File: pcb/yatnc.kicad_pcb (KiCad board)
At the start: 2 copper layers, 45 x 85 mm, 24 parts, among them J1 Conn_01x10_Socket, J3 Conn_01x02_Socket, J4 Conn_01x03_Pin, J5 Conn_02x02_Top_Bottom, J6 Conn_01x13_Socket, J7 Conn_01x13_Socket, Q1 BC547, SW1 SW_Push, U1 MAX3232

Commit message: Fix DRC errors
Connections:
- R1 pad 1: GND -> VCC
- R2 pad 2: VCC -> GND
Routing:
- net Net-(J1-Pin_8): track 45.2 -> 47.0 mm
- net VCC: track 79.3 -> 78.8 mm, vias 1 -> 0
- net GND: track 0.00 -> 0.26 mm, vias 2 -> 3

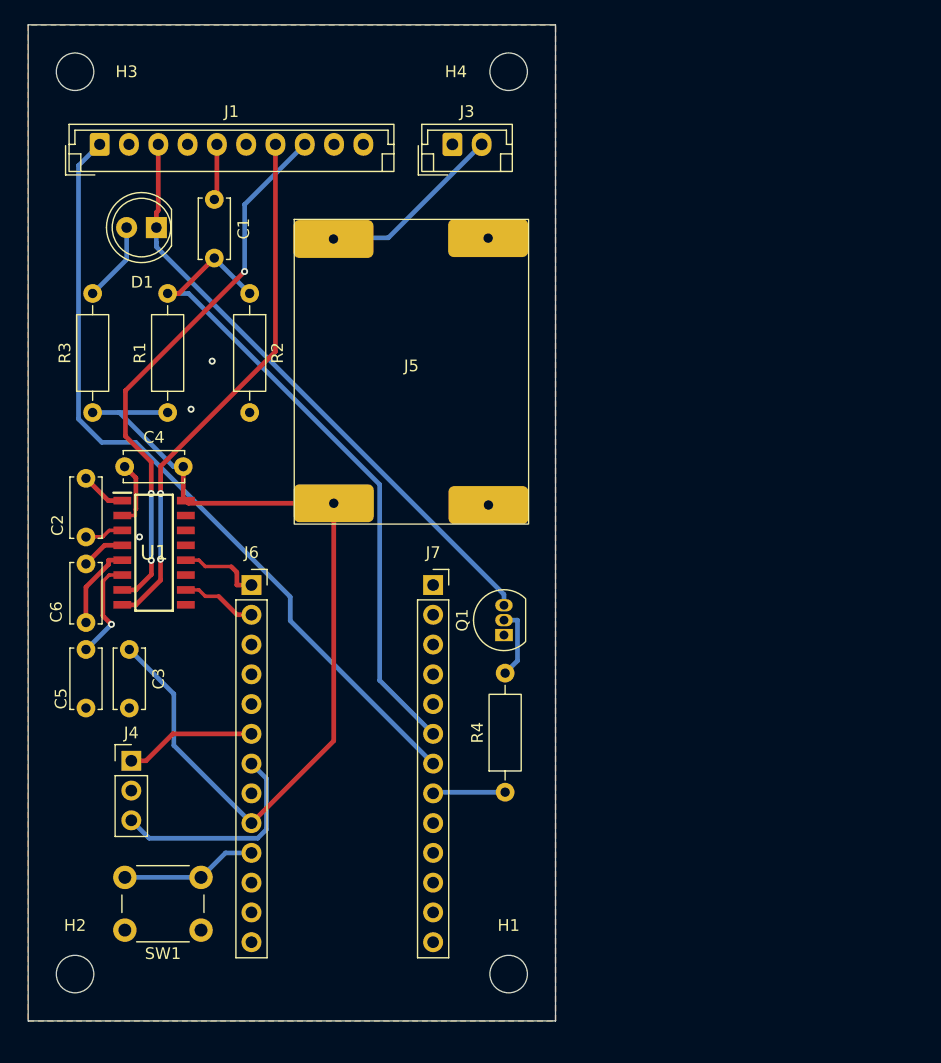
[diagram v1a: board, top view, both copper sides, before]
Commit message: add into schema 2 stage RC filter
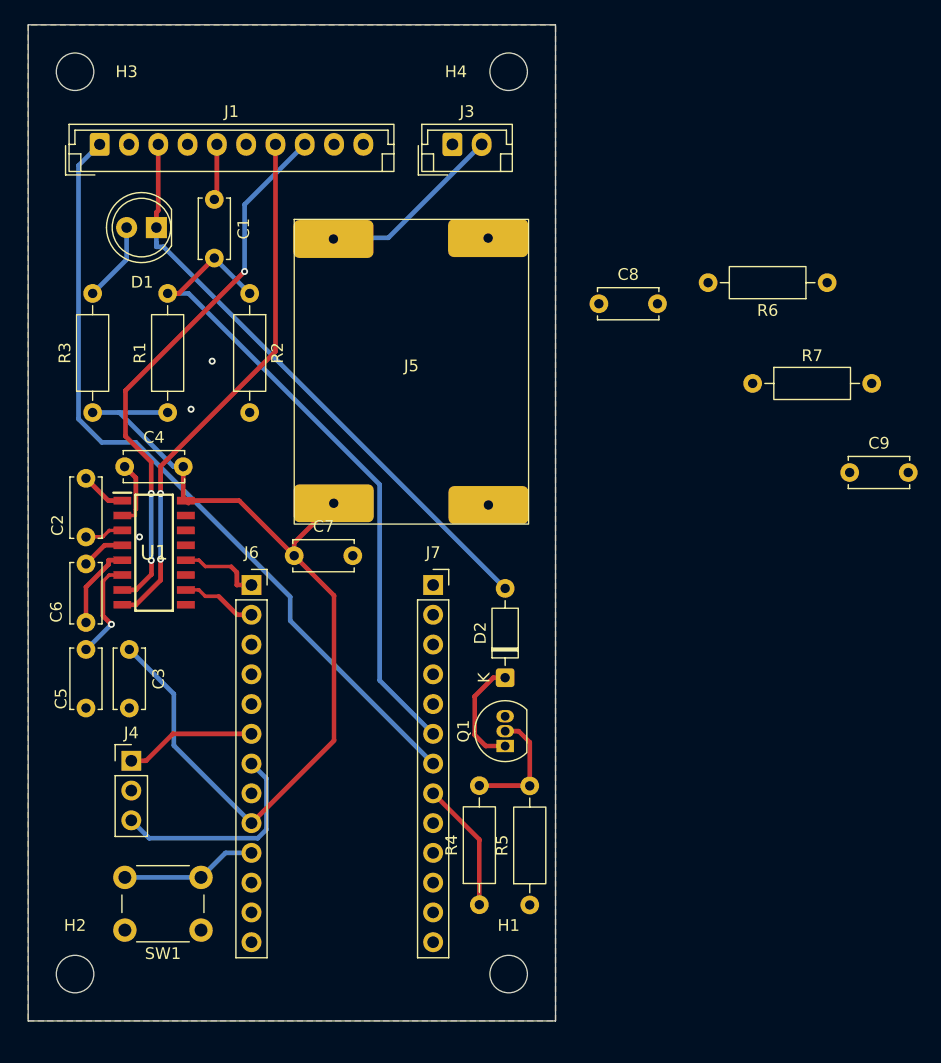
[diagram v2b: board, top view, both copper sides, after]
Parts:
- added C7: C, Capacitor_THT:C_Disc_D5.0mm_W2.5mm_P5.00mm, F.Cu at (193.2, 91.8)
- added C8: C, Capacitor_THT:C_Disc_D5.0mm_W2.5mm_P5.00mm, F.Cu at (219.2, 70.3)
- added C9: C, Capacitor_THT:C_Disc_D5.0mm_W2.5mm_P5.00mm, F.Cu at (240.6, 84.7)
- added D2: 1N4148, Diode_THT:D_DO-35_SOD27_P7.62mm_Horizontal, F.Cu at (211.2, 102.2)
- added R5: R, Resistor_THT:R_Axial_DIN0207_L6.3mm_D2.5mm_P10.16mm_Horizontal, F.Cu at (213.3, 121.6)
- added R6: R, Resistor_THT:R_Axial_DIN0207_L6.3mm_D2.5mm_P10.16mm_Horizontal, F.Cu at (238.7, 68.5)
- added R7: R, Resistor_THT:R_Axial_DIN0207_L6.3mm_D2.5mm_P10.16mm_Horizontal, F.Cu at (232.3, 77.1)
- moved R4 9.85 mm to (209.0, 121.6)
- moved Q1 9.47 mm to (211.2, 108.0)
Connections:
- J7 pad 7: Net-(J1-Pin_1) -> Net-(J7-Pin_7)
- Q1 pad 1: GND -> Net-(D2-K)
- Q1 pad 3: Net-(D1-K) -> GND
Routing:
- net Net-(D2-K): track 0.00 -> 9.55 mm
- net Net-(J7-Pin_8): track 6.19 -> 11.3 mm
- net Net-(Q1-B): track 6.11 -> 10.5 mm
- net VCC: track 78.8 -> 80.4 mm
- net Net-(D1-K): track 51.7 -> 50.6 mm

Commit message: added afsk filter and vin protection
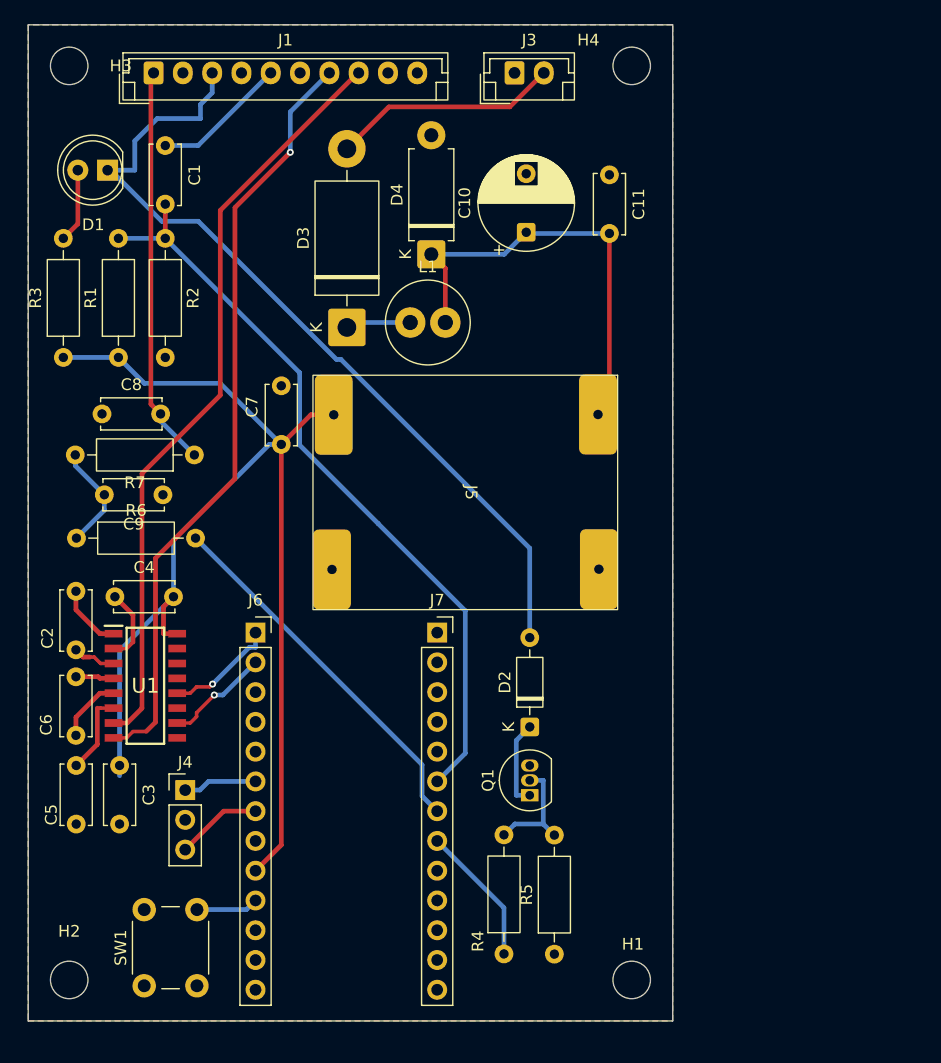
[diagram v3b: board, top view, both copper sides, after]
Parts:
- added C10: C_Polarized, Capacitor_THT:CP_Radial_D8.0mm_P5.00mm, F.Cu at (213.0, 64.2)
- added C11: C, Capacitor_THT:C_Disc_D5.0mm_W2.5mm_P5.00mm, F.Cu at (220.1, 59.3)
- added D3: 1N5822, Diode_THT:D_DO-201AD_P15.24mm_Horizontal, F.Cu at (197.7, 72.3)
- added D4: PTVS18VZ1USK, Diode_THT:D_DO-15_P10.16mm_Horizontal, F.Cu at (204.9, 66.1)
- added L1: L, Inductor_THT:L_Radial_D7.0mm_P3.00mm, F.Cu at (203.1, 71.9)
- moved R6 67.7 mm to (174.6, 90.3), turned to 0 degrees
- moved C9 58.6 mm to (182.0, 86.6), turned to 180 degrees
- moved R7 48.0 mm to (184.7, 83.2), turned to 180 degrees
- moved C8 43.4 mm to (176.8, 79.7)
- moved U1 11.4 mm to (180.5, 102.9)
- moved J5 11.3 mm to (207.8, 86.4), turned to -90 degrees
- moved C4 11.1 mm to (177.9, 95.3)
- moved H1 10.5 mm to (222.0, 128.0)
- moved H4 10.5 mm to (222.0, 50.0)
- moved C3 9.93 mm to (178.3, 109.7)
- moved C5 9.93 mm to (174.6, 109.7)
- moved C2 9.67 mm to (174.6, 94.8)
- moved C6 9.67 mm to (174.6, 102.1)
- moved C7 9.56 mm to (192.1, 82.3), turned to 90 degrees
- moved R2 8.60 mm to (182.2, 64.7)
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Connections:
- net +12V renamed Net-(D4-K)
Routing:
- net VCC: track 80.4 -> 123.2 mm
- net Net-(J1-Pin_1): track 67.8 -> 34.2 mm
- net Net-(J7-Pin_7): track 0.00 -> 31.8 mm
- net Net-(D4-K): track 15.9 -> 38.2 mm
- net Net-(D1-K): track 50.6 -> 72.1 mm
- net Net-(J1-Pin_7): track 45.4 -> 65.7 mm, vias 2 -> 1
- net Net-(J1-Pin_8): track 47.0 -> 64.9 mm, vias 3 -> 0
- net Net-(J4-Pin_3): track 18.6 -> 7.36 mm
- net Net-(C9-Pad2): track 0.00 -> 9.11 mm
- net Net-(J7-Pin_6): track 57.5 -> 64.9 mm
- net Net-(J1-Pin_5): track 4.79 -> 11.6 mm
- net Net-(J6-Pin_10): track 11.7 -> 5.32 mm
- net Net-(D3-K): track 0.00 -> 5.57 mm
- net Net-(J4-Pin_1): track 11.2 -> 6.31 mm
- net Net-(J6-Pin_2): track 6.48 -> 9.03 mm, vias 0 -> 1
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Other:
- board size 45 x 85 mm -> 55 x 85 mm

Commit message: resolve ERC/DRC. add cleaning silkscreen, add component values
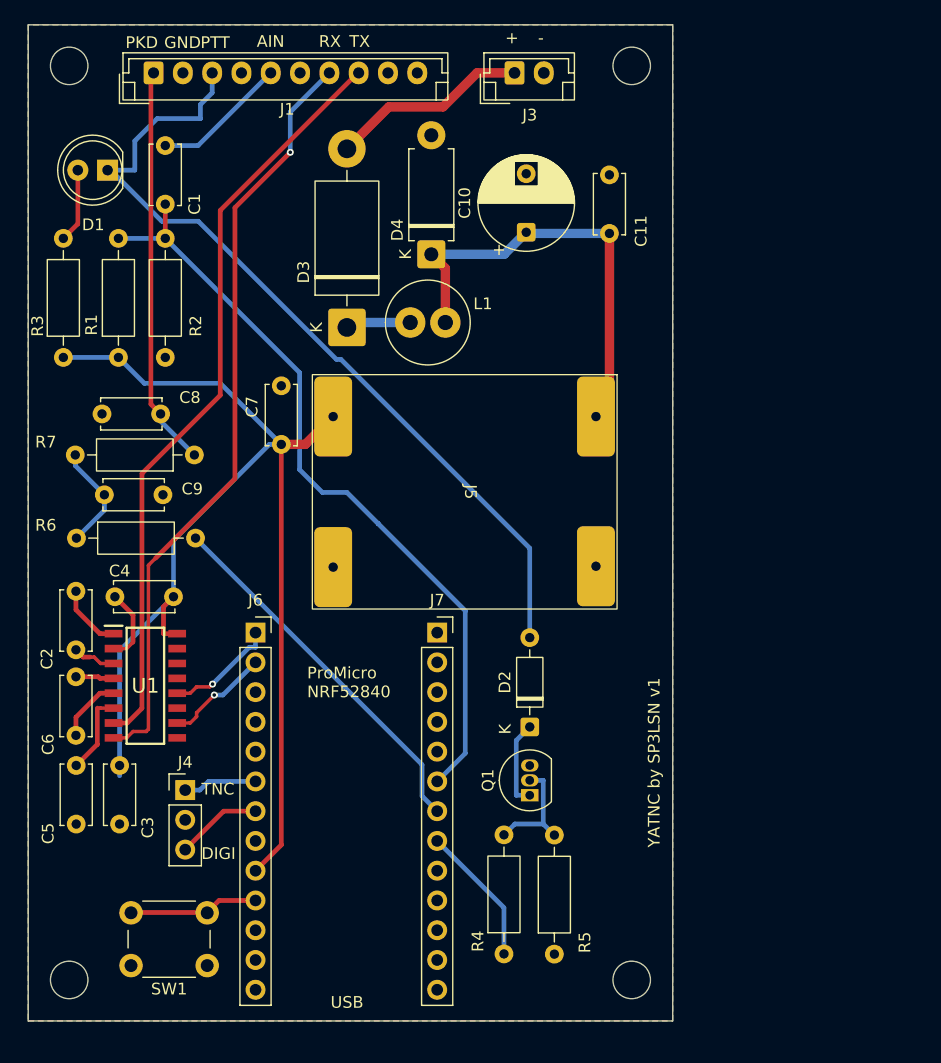
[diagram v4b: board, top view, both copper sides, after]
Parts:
- C1, C11, C2, C3, C4, C5, C6, C7: value C -> 100nF
- C10: value C_Polarized -> 470µF
- C8, C9: value C -> 4.7 nF
- D4: value PTVS18VZ1USK -> BZW04
- J5: value Conn_02x02_Top_Bottom -> DFR0570
- L1: value L -> 47µH
- R1, R2, R3, R5: value R -> 10k
- R4, R6, R7: value R -> 1k
- moved SW1 5.65 mm to (185.8, 126.8), turned to 180 degrees
- moved J5 0.07 mm to (207.8, 86.3)
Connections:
- D3 pad 2: VCC -> Net-(D3-A)
- J3 pad 1: GND -> Net-(D3-A)
- J3 pad 2: Net-(D4-K) -> GND
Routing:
- net VCC: track 123.2 -> 103.6 mm
- net Net-(D3-A): track 0.00 -> 17.0 mm
- net Net-(J6-Pin_10): track 5.32 -> 11.1 mm
- net Net-(D4-K): track 38.2 -> 36.8 mm
- net Net-(J7-Pin_6): track 64.9 -> 66.1 mm
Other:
- board text added: "+"
- board text added: "-"
- board text added: "AIN"
- board text added: "DIGI"
- board text added: "GND"
- board text added: "PKD"
- board text added: "PTT"
- board text added: "ProMicro NRF52840"
- board text added: "RX"
- board text added: "TNC"
- board text added: "TX"
- board text added: "USB"
- board text added: "YATNC by SP3LSN v1"

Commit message: first part of changes after review
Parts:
- removed L1: 47µH, Inductor_THT:L_Radial_D7.0mm_P3.00mm
- added R8: 1ohm, Resistor_THT:R_Axial_DIN0207_L6.3mm_D2.5mm_P10.16mm_Horizontal, F.Cu at (202.8, 74.2)
- D4: value BZW04 -> BZW04 18V
- J1: value Conn_01x10_Socket -> JST
- RST: renamed from SW1; value SW_Push -> RST
- moved C11 9.43 mm to (220.9, 68.7)
- moved D3 6.68 mm to (204.1, 70.4)
- moved D4 5.30 mm to (209.4, 68.9)
- moved C10 3.70 mm to (216.5, 63.0), turned to 0 degrees
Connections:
- net Net-(D1-K) renamed PTT
- net Net-(J1-Pin_1) renamed PKD
- net Net-(J1-Pin_5) renamed AUDIO IN
- net Net-(J4-Pin_1) renamed TNC
- net Net-(J4-Pin_3) renamed DIGI
- net Net-(J7-Pin_7) renamed AUDIO OUT
- net VCC renamed 3.3V
- J1 pad 7: Net-(J1-Pin_7) -> RX
- J1 pad 8: Net-(J1-Pin_8) -> TX
- U1 pad 11: unconnected-(U1-T1IN-Pad11) -> Net-(J6-Pin_2)
- U1 pad 13: unconnected-(U1-R1IN-Pad13) -> RX
- U1 pad 14: unconnected-(U1-T1OUT-Pad14) -> TX
- U1 pad 7: Net-(J1-Pin_8) -> TX
- U1 pad 8: Net-(J1-Pin_7) -> GND
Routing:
- net TX: track 0.00 -> 70.2 mm
- net Net-(J1-Pin_7): track 65.7 -> 0.00 mm, vias 1 -> 0
- net Net-(J1-Pin_8): track 64.9 -> 0.00 mm
- net RX: track 0.00 -> 64.1 mm
- net Net-(D3-A): track 17.0 -> 9.80 mm
- net Net-(D3-K): track 5.57 -> 4.31 mm
- net Net-(D4-K): track 36.8 -> 35.9 mm
- net Net-(J6-Pin_1): track 9.56 -> 8.83 mm, vias 1 -> 0
- net Net-(J6-Pin_2): track 9.03 -> 9.58 mm, vias 1 -> 0
- net GND: vias 0 -> 103

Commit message: second part of changes after review
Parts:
- removed the C7 at (192.1, 82.3)
- added C4: 100nF, Capacitor_THT:C_Disc_D5.0mm_W2.5mm_P5.00mm, F.Cu at (198.7, 124.0)
- added C6: 470µF, Capacitor_THT:CP_Radial_D8.0mm_P5.00mm, F.Cu at (199.6, 93.6)
- added POWER LED: LED, LED_THT:LED_D5.0mm, F.Cu at (177.2, 58.9)
- added R1: 10k, Resistor_THT:R_Axial_DIN0207_L6.3mm_D2.5mm_P10.16mm_Horizontal, F.Cu at (173.5, 74.8)
- BC547: renamed from Q1; footprint Package_TO_SOT_THT:TO-92_Inline -> Package_TO_SOT_THT:TO-92_Inline_Wide
- PTT LED: renamed from D1
- TO TRANSCEIVER: renamed from J1
- moved R6 27.0 mm to (219.8, 99.1), turned to -90 degrees
- moved D2 23.6 mm to (223.1, 56.4), turned to 180 degrees
- moved R2 20.5 mm to (221.8, 66.3), turned to 180 degrees
- moved C2 19.8 mm to (202.1, 74.9), turned to 90 degrees
- moved C9 18.3 mm to (186.4, 93.3)
- moved C1 11.3 mm to (205.7, 66.4), turned to 90 degrees
- moved R5 9.45 mm to (219.8, 122.1)
- moved DFR0570 7.59 mm to (214.1, 82.2), turned to 0 degrees
- moved D3 7.16 mm to (211.7, 62.1), turned to 0 degrees
- moved PTT LED 7.00 mm to (184.3, 58.9)
- moved C7 5.90 mm to (188.1, 56.8)
- moved R7 4.70 mm to (178.2, 74.8)
- moved R8 4.50 mm to (186.7, 64.6)
- moved R9 4.50 mm to (182.7, 74.8)
- moved J5 4.12 mm to (194.0, 98.7)
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- renumbered C10 to C1, C4 to C10, C5 to C11, C6 to C12, C11 to C2, C8 to C3, C9 to C5, C1 to C7, C2 to C8, C3 to C9, D3 to D2, D4 to D3, D2 to D5, J5 to DFR0570, H2 to H1, H1 to H2, J4 to J1, J6 to J5, J7 to J6, J3 to PWR, R8 to R2, R7 to R3, R6 to R4, R4 to R5, R5 to R6, R3 to R7, R2 to R8, R1 to R9
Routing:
- net Net-(D3-K): track 35.9 -> 24.6 mm
- net PTT: track 72.1 -> 64.4 mm, vias 0 -> 2
- net Net-(D2-K): track 4.31 -> 11.5 mm
- net AUDIO OUT: track 31.8 -> 38.6 mm, vias 0 -> 1
- net Net-(J5-Pin_2): track 9.58 -> 15.8 mm
- net Net-(D1-A): track 0.00 -> 6.19 mm
- net TNC: track 6.31 -> 11.5 mm
- net DIGI: track 7.36 -> 12.6 mm
- net AUDIO IN: track 11.6 -> 7.48 mm
- net PKD: track 34.2 -> 38.3 mm, vias 0 -> 5
- net RX: track 64.1 -> 60.2 mm, vias 0 -> 2
- net Net-(J5-Pin_1): track 8.83 -> 12.8 mm
- net Net-(D5-K): track 7.46 -> 10.5 mm
- net Net-(Q1-B): track 9.95 -> 7.31 mm
- net TX: track 70.2 -> 67.7 mm, vias 0 -> 2
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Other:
- outline, holes or cut-outs redrawn

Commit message: added OSHW logo
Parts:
- added REF**: OSHW-Logo_11.4x12mm_SilkScreen, Symbol:OSHW-Logo_11.4x12mm_SilkScreen, F.Cu at (194.8, 76.9)
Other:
- board text added: "YATNC by SP3LSN V1.0"
- board text removed: "YATNC by SP3LSN v1"

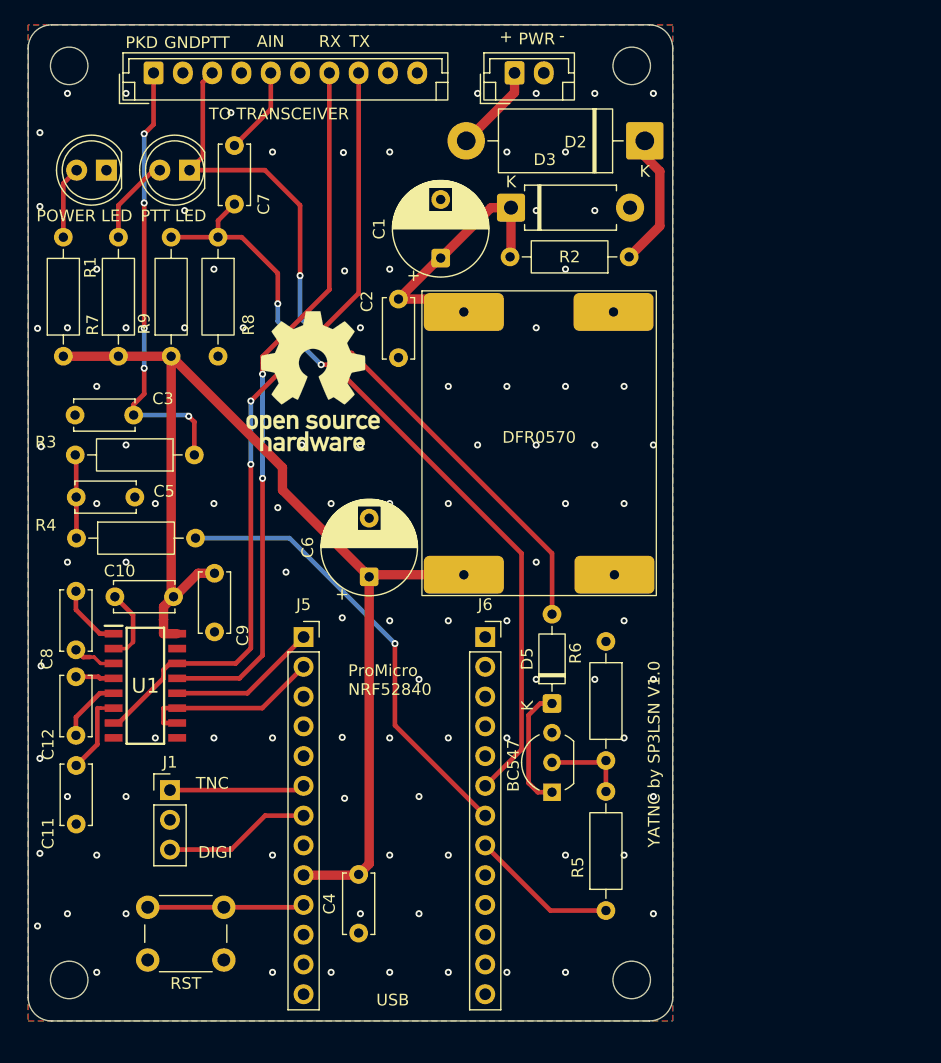
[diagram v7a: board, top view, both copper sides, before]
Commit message: added GPS
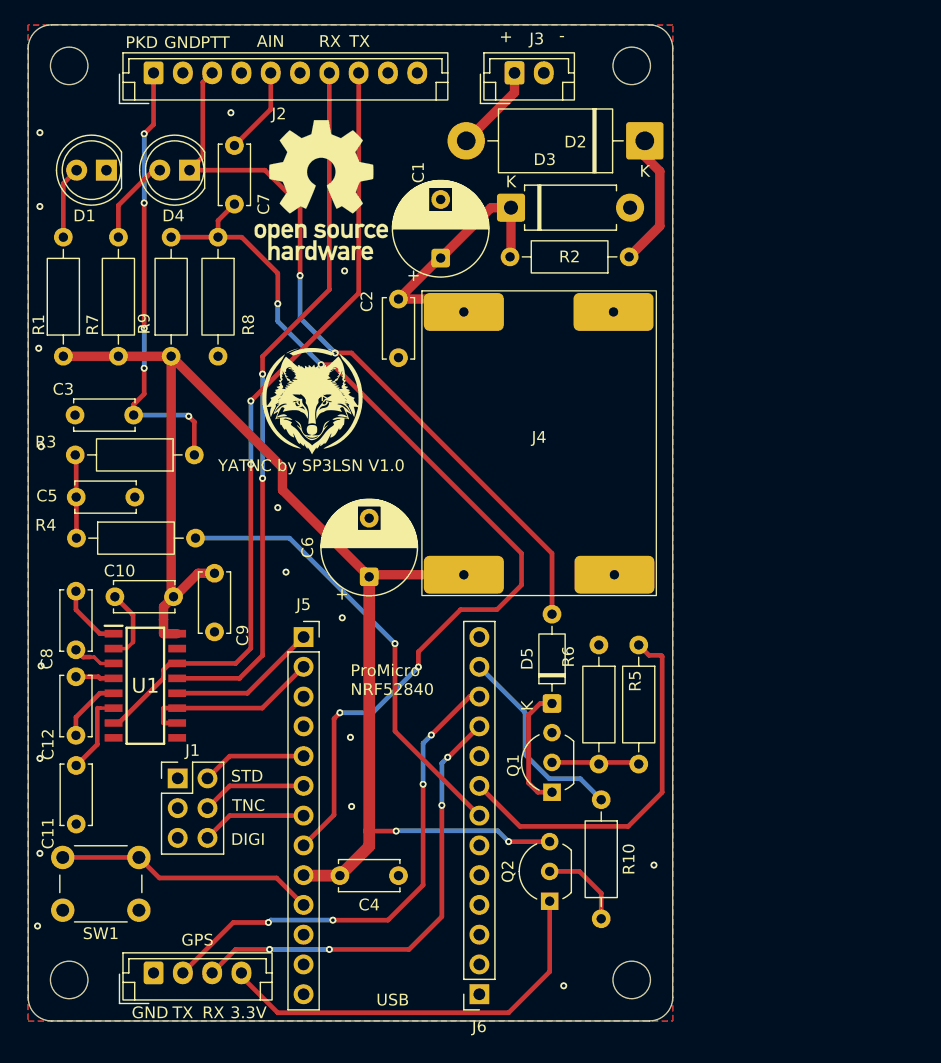
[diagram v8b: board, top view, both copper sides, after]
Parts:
- added G***: LOGO, images:logo_small, F.Cu at (194.8, 78.5)
- added GPS: GPS, Connector_JST:JST_EH_B4B-EH-A_1x04_P2.50mm_Vertical, F.Cu at (181.2, 127.4)
- added Q2: BC547, Package_TO_SOT_THT:TO-92_Inline_Wide, F.Cu at (215.0, 121.3)
- added R10: 1k, Resistor_THT:R_Axial_DIN0207_L6.3mm_D2.5mm_P10.16mm_Horizontal, F.Cu at (219.4, 112.6)
- D1: renamed from POWER LED
- D4: renamed from PTT LED
- J1: value Conn_01x03_Pin -> Conn_02x03_Top_Bottom; footprint Connector_PinHeader_2.54mm:PinHeader_1x03_P2.54mm_Vertical -> Connector_PinHeader_2.54mm:PinHeader_2x03_P2.54mm_Vertical
- J2: renamed from TO TRANSCEIVER
- moved J6 30.5 mm to (209.0, 129.2), turned to 180 degrees
- moved R5 22.8 mm to (222.6, 99.4), turned to -90 degrees
- moved REF** 16.3 mm to (195.5, 60.6)
- moved SW1 8.40 mm to (179.9, 122.0)
- moved C4 5.96 mm to (202.1, 119.1), turned to 180 degrees
- moved J1 1.20 mm to (183.3, 110.8)
- moved R6 0.67 mm to (219.2, 99.4)
- renumbered PWR to J3, DFR0570 to J4, BC547 to Q1, RST to SW1
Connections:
- C7 pad 1: AUDIO IN -> AUDIO TRCV
- C7 pad 2: Net-(J6-Pin_6) -> AUDIO IN
- J1 pad 1: TNC -> GND
- J1 pad 2: GND -> STD
- J1 pad 3: DIGI -> GND
- J2 pad 5: AUDIO IN -> AUDIO TRCV
- J5 pad 5: unconnected-(J5-Pin_5-Pad5) -> STD
- J5 pad 8: unconnected-(J5-Pin_8-Pad8) -> AUDIO IN
- J6 pad 10: unconnected-(J6-Pin_10-Pad10) -> GPS RX
- J6 pad 11: unconnected-(J6-Pin_11-Pad11) -> GPS TX
- J6 pad 12: unconnected-(J6-Pin_12-Pad12) -> GPS EN
- J6 pad 6: Net-(J6-Pin_6) -> unconnected-(J6-Pin_6-Pad6)
- R8 pad 1: Net-(J6-Pin_6) -> AUDIO IN
- R9 pad 2: Net-(J6-Pin_6) -> AUDIO IN
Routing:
- net AUDIO IN: track 7.48 -> 83.0 mm, vias 0 -> 4
- net Net-(J6-Pin_6): track 68.0 -> 0.00 mm, vias 2 -> 0
- net GPS TX: track 0.00 -> 42.2 mm, vias 0 -> 4
- net GPS RX: track 0.00 -> 39.2 mm, vias 0 -> 4
- net Net-(J7-Pin_4): track 0.00 -> 35.4 mm
- net Net-(J6-Pin_8): track 12.6 -> 32.2 mm
- net GPS EN: track 0.00 -> 17.2 mm
- net 3.3V: track 104.0 -> 118.9 mm, vias 0 -> 2
- net STD: track 0.00 -> 8.99 mm
- net Net-(J5-Pin_10): track 13.4 -> 22.2 mm
- net AUDIO TRCV: track 0.00 -> 7.48 mm
- net Net-(Q2-B): track 0.00 -> 7.35 mm
- net DIGI: track 12.6 -> 8.99 mm
- net TNC: track 11.5 -> 9.50 mm
- net GND: vias 101 -> 18
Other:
- board text added: "3.3V"
- board text added: "STD"
